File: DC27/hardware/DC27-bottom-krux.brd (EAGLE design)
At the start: 102.4 x 117.6 mm, 95 parts, among them IC2 LDL112D33R, IC3 FT2232HL-REEL, IC4 93LC46BT-I_OT, J1 PAIRING, J2 JTAG, J3 Battery, J4 Program Port, U2 ESP-WROOM-32, Y1 ABM7-12.000MHZ-D2Y-T

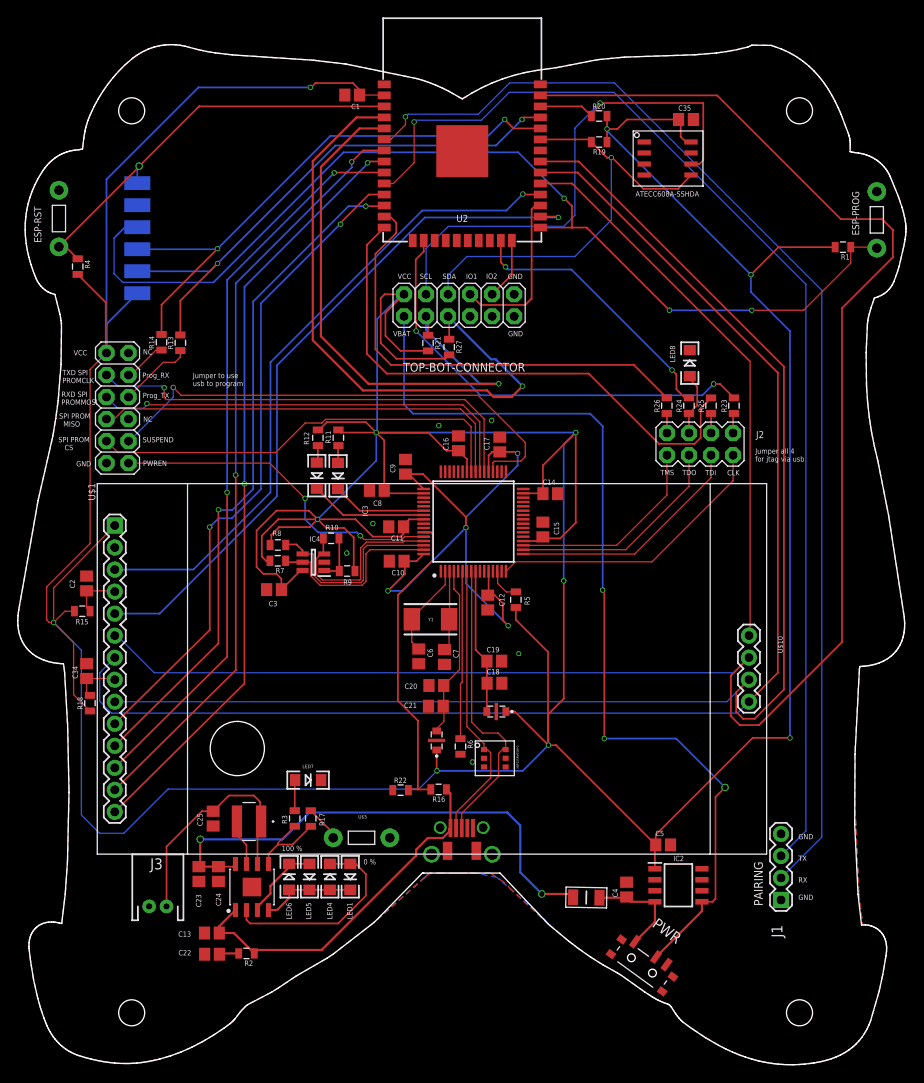
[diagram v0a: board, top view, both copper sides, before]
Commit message: Added puzzle elemenets for Krux's Challenge.
Added puzzle elemenets for Krux's Challenge.  Cleaned up size/font/position for part labels
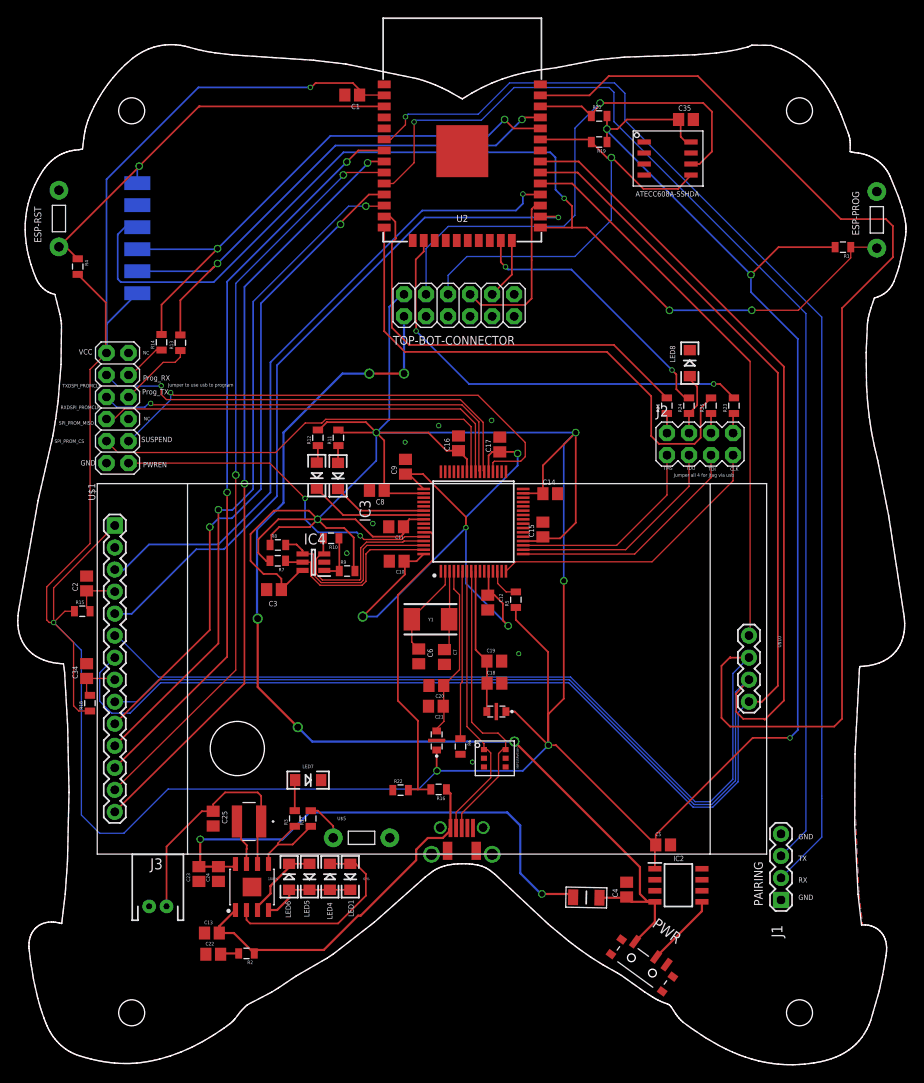
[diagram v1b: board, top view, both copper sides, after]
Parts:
- removed R21, R27: 10 K, dc-26:0805
- removed U$13: DC27_PUZZLE_ELEMENT_4, darknet_parts_library:DC27_PUZZLE_ELEMENT_4
- removed U$14: DC27_PUZZLE_ELEMENT_5, darknet_parts_library:DC27_PUZZLE_ELEMENT_5
- removed U$15: DC27_PUZZLE_ELEMENT_6, darknet_parts_library:DC27_PUZZLE_ELEMENT_6
- U$12: value DC27_PUZZLE_ELEMENT_3 -> KRUX_LOGO; device darknet_parts_library:DC27_PUZZLE_ELEMENT_3 -> darknet_parts_library:KRUX_LOGO
- U$7: value KRUX_LOGO -> DC27_PUZZLE_ELEMENT_3; device logos:KRUX_LOGO -> darknet_parts_library:DC27_PUZZLE_ELEMENT_3
- moved U$12 64.6 mm to (10.4, 13.1)
- moved U$7 62.6 mm to (74.4, 21.0)
- moved U$11 2.47 mm to (30.5, 76.8)
- moved U$6 0.51 mm to (79.6, 88.4)
- moved C22 0.14 mm to (22.5, 12.7)
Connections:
- net EN: no longer TOP-BOT-CONNECTOR.1
- net SVN: no longer R21.1, TOP-BOT-CONNECTOR.3
- net SVP: no longer R27.1, TOP-BOT-CONNECTOR.5
- net TOUCH_DATA_IN: now also U2.7; no longer U2.9
- net TOUCH_DATA_OUT: now also U2.9; no longer U2.7
- net VBAT: now also TOP-BOT-CONNECTOR.1
- net VCC: no longer R21.2, R27.2
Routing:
- net VBAT: track 12.2 -> 124.0 mm, vias 0 -> 5
- net EN: track 110.0 -> 8.55 mm, vias 3 -> 0
- net SVP: track 73.0 -> 0.00 mm, vias 1 -> 0
- net SVN: track 66.2 -> 0.00 mm, vias 1 -> 0
- net DISPLAY_SD_MOSI: track 197.5 -> 227.3 mm
- net VCC: track 641.5 -> 615.9 mm
- net DISPLAY_SD_MISO: track 160.8 -> 179.5 mm
- net DISPLAY_SD_SCK: track 158.0 -> 175.4 mm
- net VCC1.8: track 69.5 -> 77.8 mm
- net JTAG_TMS: track 53.2 -> 49.0 mm
- net N$20: track 27.4 -> 29.2 mm
- net JTAG_TDI: track 63.6 -> 61.9 mm
- net ESP-IO0: track 118.7 -> 120.2 mm
- net TOUCH_DATA_OUT: track 88.1 -> 86.7 mm
- net JTAG_CLK: track 51.8 -> 50.7 mm
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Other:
- outline, holes or cut-outs redrawn
- board text added: "PLY OTIS GIST DADE PEW HIP RAM LAIN GIST DADE PEW PEP RAP KEN GLUM CRUD CARE PAY RAM LAIN GIST CREW FOAL HAD REP HOLE GIST DADE LAY HID RAM GATE GLOW CAVE ARM HOOF RAM NAIR GLUM CREW HANG HOFF PAR FLAG AMOS COAT CARD HEM REP HOLE GYP COME VAN HOW RAM LAIN GIST DADE PEW HUH REP JILT GLUM CAVE ARM HUNT RAP PAL REAL CAVE ARM HOLM RAM LAIR GLUM CRUD LAP GYM RAM OTTO RATE CAVE ARM HI RAM GATE RARE CRU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"
- board text added: "RXDSPI_PROMCLK"
- board text added: "SMALL HIGH LIGATURE QAF WITH LAM WITH ALEF MAKSURA"
- board text added: "SPI_PROM_CS"
- board text added: "SPI_PROM_MISO"
- board text added: "TXDSPI_PROMCLK"
- board text removed: "Greetings Agent. Can you solve my Challenge?"
- board text removed: "IO1"
- board text removed: "IO2"
- board text removed: "RXD SPI PROMMOSI"
- board text removed: "SCL"
- board text removed: "SDA"
- board text removed: "SPI PROM CS"
- board text removed: "SPI PROM MISO"
- board text removed: "TXD SPI PROMCLK"
- board text removed: "VBAT"
